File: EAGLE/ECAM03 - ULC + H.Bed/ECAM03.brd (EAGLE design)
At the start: 160 x 60 mm, 55 parts, among them J1 MODULAR TOOL, J2 FAN1, J3 FAN2, J4 FAN3, J5 B4B-PH-SM4, J6 SSR, J7 RINGLIGHT, J8 FTDI, J9 SPI, Q2 16MHz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

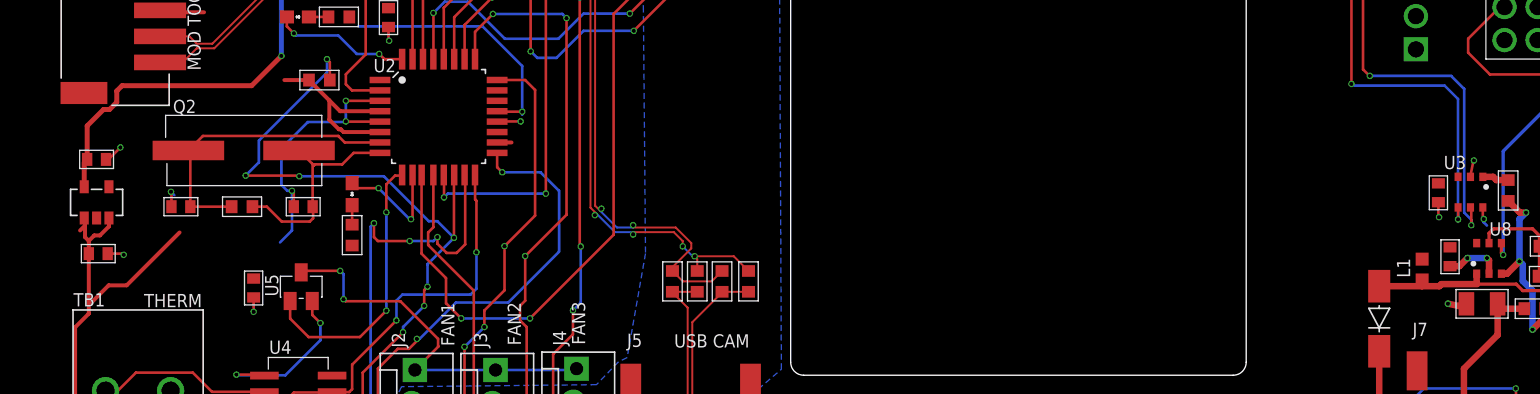
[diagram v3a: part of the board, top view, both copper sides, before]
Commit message: Resistance check, minor changes to EFP01 BOM (100 Ohm changed to 120 Ohm)
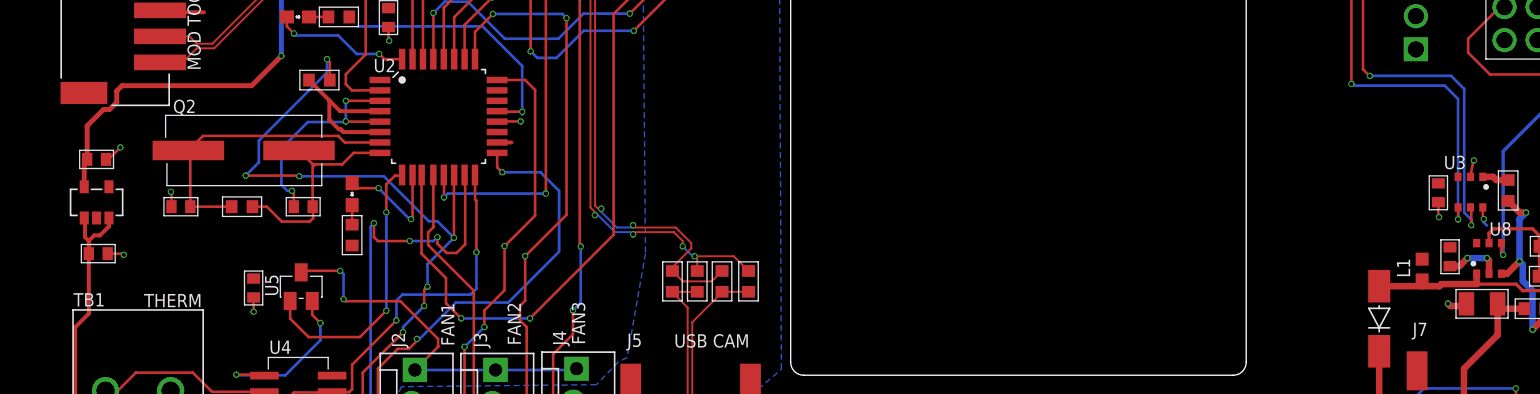
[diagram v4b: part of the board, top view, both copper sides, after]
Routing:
- net +5V: track 72.5 -> 60.8 mm
- net GND: track 145.1 -> 140.5 mm
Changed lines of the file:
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@@
 <wire x1="19.9136" y1="12.5476" x2="21.9872" y2="12.5476" width="0.2032" layer="1"/>
 <wire x1="21.9872" y1="12.5476" x2="22.0634" y2="12.4714" width="0.2032" layer="1"/>
-<wire x1="15.1384" y1="26.3398" x2="14.8844" y2="26.5938" width="0.2032" layer="16"/>
+<wire x1="15.1384" y1="26.3398" x2="14.8844" y2="26.5938" width="0" layer="19" extent="1-16"/>
 <wire x1="23.368" y1="29.9212" x2="25.4" y2="31.9532" width="0.2032" layer="16"/>
 <wire x1="25.4" y1="31.9532" x2="28.2702" y2="31.9532" width="0.2032" layer="16"/>
@@
 <wire x1="17.3228" y1="46.5328" x2="17.5387" y2="46.5328" width="0.2032" layer="16"/>
 <wire x1="17.5387" y1="46.5328" x2="20.3835" y2="43.688" width="0.2032" layer="16"/>
-<wire x1="23.2664" y1="22.7076" x2="24.1808" y2="23.622" width="0.2032" layer="16"/>
-<wire x1="24.1808" y1="23.622" x2="24.1808" y2="26.67" width="0.2032" layer="16"/>
 <via x="24.1808" y="26.67" extent="1-16" drill="0.3048"/>
 <wire x1="24.1808" y1="26.67" x2="24.3194" y2="26.5314" width="0.2032" layer="1"/>
@@
 <wire x1="116" y1="21.5" x2="114.5" y2="21.5" width="0.5" layer="16"/>
 <wire x1="114.4208" y1="17.9846" x2="113.8208" y2="17.8208" width="0.5" layer="1"/>
-<wire x1="113.8208" y1="17.8208" x2="113" y2="18" width="0.5" layer="1"/>
 <via x="113" y="18" extent="1-16" drill="0.3048"/>
 <wire x1="40.4305" y1="32.785" x2="40.4655" y2="32.75" width="0.2032" layer="1"/>
@@
 <wire x1="53.2892" y1="50.6984" x2="53.0352" y2="50.6984" width="0.2032" layer="16"/>
 <wire x1="53.0352" y1="50.6984" x2="49.8856" y2="47.5488" width="0.2032" layer="16"/>
+<wire x1="113.8208" y1="17.8208" x2="113.1792" y2="17.8208" width="0.508" layer="1"/>
+<wire x1="113.1792" y1="17.8208" x2="113" y2="18" width="0.508" layer="1"/>
 </signal>
 <signal name="+5V">
@@
 <wire x1="8.5714" y1="21.844" x2="8.5714" y2="22.823" width="0.3048" layer="1"/>
 <wire x1="8.5714" y1="22.823" x2="8.2804" y2="23.114" width="0.3048" layer="1"/>
-<wire x1="8.2804" y1="23.114" x2="8.2804" y2="24.003" width="0.3048" layer="1"/>
-<wire x1="8.2804" y1="24.003" x2="8.2804" y2="24.52" width="0.3048" layer="1"/>
+<wire x1="8.2804" y1="23.114" x2="8.2804" y2="24.52" width="0.3048" layer="1"/>
+<wire x1="8.2804" y1="24.003" x2="8.2804" y2="24.52" width="0" layer="19" extent="1-16"/>
 <wire x1="8.2804" y1="24.52" x2="8.2194" y2="24.581" width="0.3048" layer="1"/>
-<wire x1="8.5714" y1="21.844" x2="8.5714" y2="17.8816" width="0.3048" layer="1"/>
-<wire x1="8.5714" y1="17.8816" x2="8.5714" y2="17.235" width="0.3048" layer="1"/>
+<wire x1="8.5714" y1="21.844" x2="8.5714" y2="17.235" width="0.3048" layer="1"/>
+<wire x1="8.5714" y1="17.8816" x2="8.5714" y2="17.235" width="0" layer="19" extent="1-16"/>
 <wire x1="10.1194" y1="24.581" x2="10.1194" y2="23.937" width="0.3048" layer="1"/>
 <wire x1="10.1194" y1="23.937" x2="9.4234" y2="23.241" width="0.3048" layer="1"/>
 <wire x1="9.4234" y1="23.241" x2="8.9894" y2="23.241" width="0.3048" layer="1"/>
 <wire x1="8.9894" y1="23.241" x2="8.5714" y2="22.823" width="0.3048" layer="1"/>
-<wire x1="7.8994" y1="23.622" x2="8.2804" y2="24.003" width="0.3048" layer="1"/>
+<wire x1="7.8994" y1="23.622" x2="8.2804" y2="24.003" width="0" layer="19" extent="1-16"/>
 <wire x1="30.9457" y1="32.785" x2="27.883" y2="32.785" width="0.3048" layer="1"/>
 <wire x1="27.883" y1="32.785" x2="27.051" y2="33.617" width="0.3048" layer="1"/>
@@
 <wire x1="7.5184" y1="9.2964" x2="7.5184" y2="16.182" width="0.3048" layer="1"/>
 <wire x1="7.5184" y1="16.182" x2="8.5714" y2="17.235" width="0.3048" layer="1"/>
-<wire x1="25.489" y1="35.179" x2="23.5966" y2="35.179" width="0.3048" layer="1"/>
-<wire x1="15.5448" y1="23.4696" x2="11.4808" y2="19.4056" width="0.3048" layer="1"/>
-<wire x1="11.4808" y1="19.4056" x2="10.0954" y2="19.4056" width="0.3048" layer="1"/>
-<wire x1="10.0954" y1="19.4056" x2="8.5714" y2="17.8816" width="0.3048" layer="1"/>
+<wire x1="15.5448" y1="23.4696" x2="11.4808" y2="19.4056" width="0" layer="19" extent="1-16"/>
+<wire x1="11.4808" y1="19.4056" x2="10.0954" y2="19.4056" width="0" layer="19" extent="1-16"/>
+<wire x1="10.0954" y1="19.4056" x2="8.5714" y2="17.8816" width="0" layer="19" extent="1-16"/>
 <wire x1="27.051" y1="32.131" x2="27.7876" y2="31.3944" width="0.3048" layer="1"/>
 <wire x1="27.7876" y1="31.3944" x2="27.94" y2="31.3944" width="0.3048" layer="1"/>
